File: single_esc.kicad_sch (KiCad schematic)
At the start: 37 parts, among them T201 BC847, T202 BC847, T203 BC847, U201 EFM8BB10

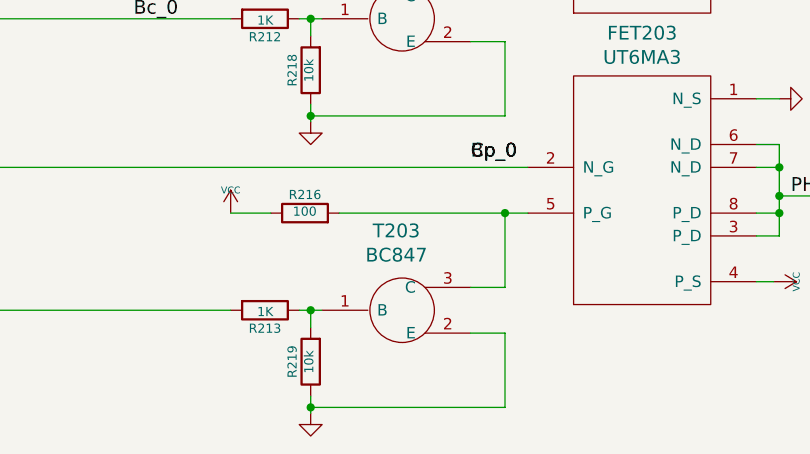
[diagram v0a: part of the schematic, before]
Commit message: made a new schematic with individual FETs
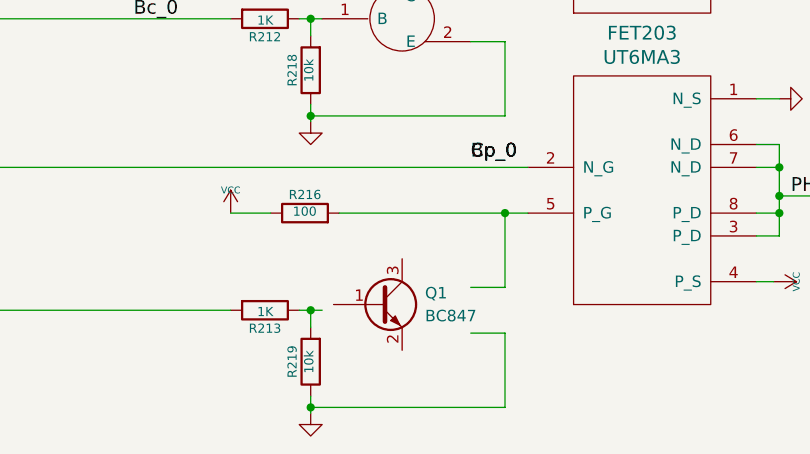
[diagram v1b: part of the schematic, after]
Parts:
- removed T203: BC847, custom:SC75, symbol custom:NPN
- added Q1: BC847, Package_TO_SOT_SMD:SOT-23, symbol Transistor_BJT:BC847
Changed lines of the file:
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@@
-    )
-  )
-  (symbol (lib_id "custom:NPN") (at 171.45 150.495 0) (unit 1)
-    (in_bom yes) (on_board yes) (dnp no)
-    (property "Reference" "T203" (at 170.815 141.6812 0)
-      (effects (font (size 1.524 1.524)))
-    )
-    (property "Value" "BC847" (at 170.815 144.3736 0)
-      (effects (font (size 1.524 1.524)))
-    )
-    (property "Footprint" "custom:SC75" (at 170.18 150.495 0)
-      (effects (font (size 1.524 1.524)) hide)
-    )
-    (property "Datasheet" "" (at 170.18 150.495 0)
-      (effects (font (size 1.524 1.524)) hide)
-    )
-    (pin "1")
-    (pin "2")
-    (pin "3")
-    (instances
-      (project "single_esc"
-        (path "/f22a7b6c-63bc-4e09-8e0c-74ca594f4985"
-          (reference "T203") (unit 1)
-        )
-      )
     )
   )
@@
         )
       )
+    )
+  )
+  (symbol (lib_id "Transistor_BJT:BC847") (at 168.91 149.86 0) (unit 1)
+    (in_bom yes) (on_board yes) (dnp no) (fields_autoplaced)
+    (property "Reference" "Q1" (at 173.99 148.59 0)
+      (effects (font (size 1.27 1.27)) (justify left))
+    )
+    (property "Value" "BC847" (at 173.99 151.13 0)
+      (effects (font (size 1.27 1.27)) (justify left))
+    )
+    (property "Footprint" "Package_TO_SOT_SMD:SOT-23" (at 173.99 151.765 0)
+      (effects (font (size 1.27 1.27) italic) (justify left) hide)
+    )
+    (property "Datasheet" "http://www.infineon.com/dgdl/Infineon-BC847SERIES_BC848SERIES_BC849SERIES_BC850SERIES-DS-v01_01-en.pdf?fileId=db3a304314dca389011541d4630a1657" (at 168.91 149.86 0)
+      (effects (font (size 1.27 1.27)) (justify left) hide)
+    )
+    (pin "1")
+    (pin "2")
+    (pin "3")
+    (instances
+      (project "single_esc"
+        (path "/f22a7b6c-63bc-4e09-8e0c-74ca594f4985"
+          (reference "Q1") (unit 1)
+        )
+      )
